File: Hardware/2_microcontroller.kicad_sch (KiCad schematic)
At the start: 27 parts, among them Y1 8Mhz

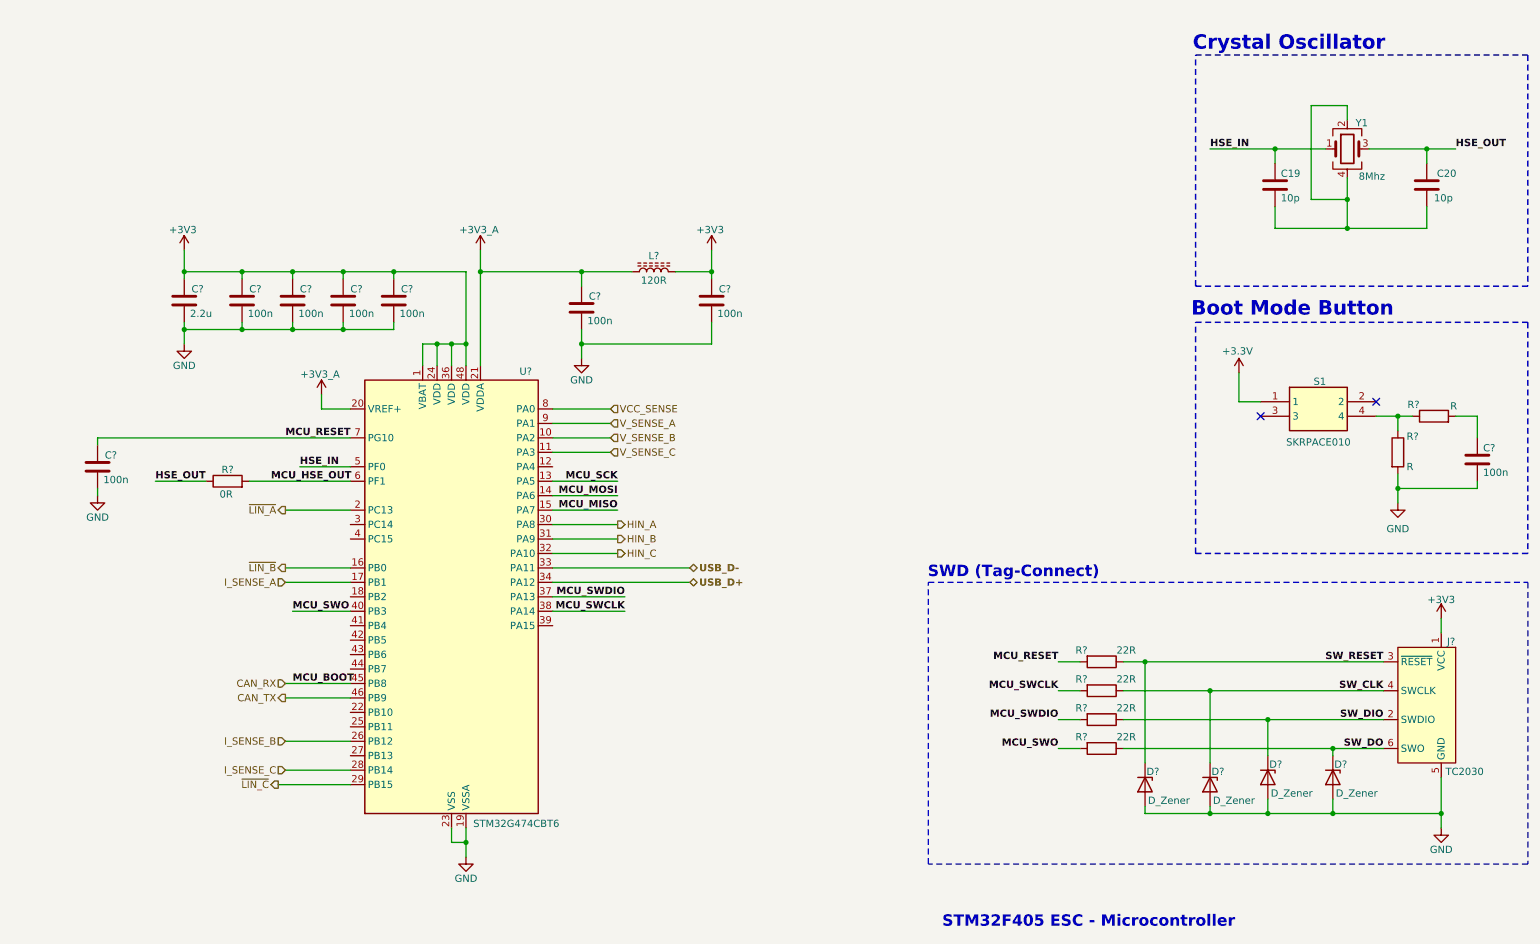
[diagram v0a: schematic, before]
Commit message: feat: Update to use I2C stemma connector
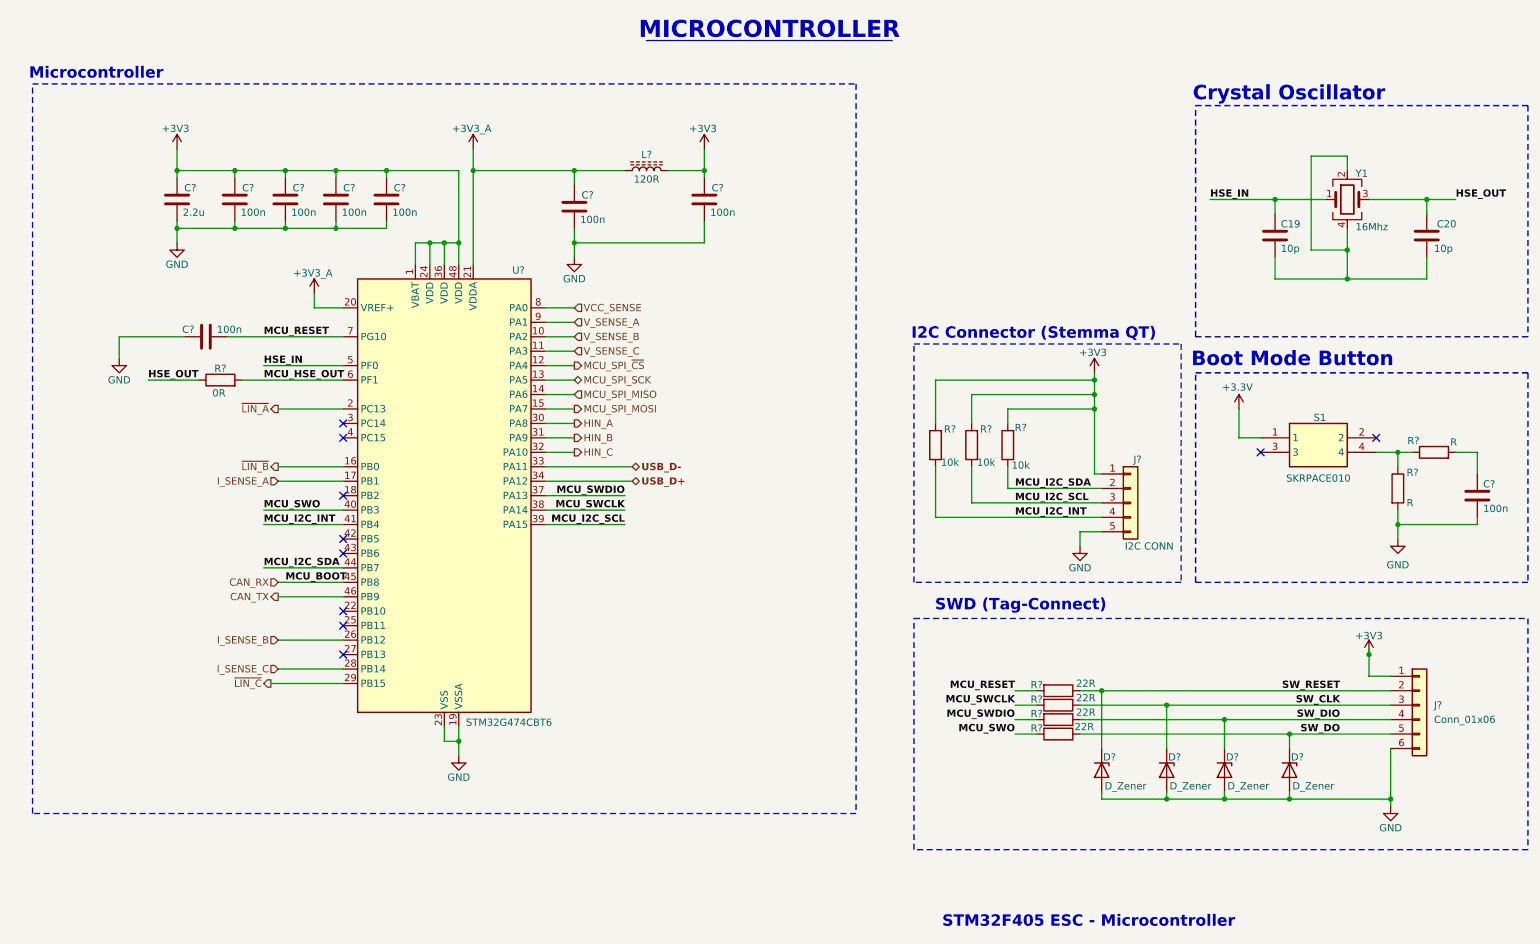
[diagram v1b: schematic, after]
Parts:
- removed J?: TC2030, Connector:Tag-Connect_TC2030-IDC-FP_2x03_P1.27mm_Vertical, symbol Connector:Conn_ARM_SWD_TagConnect_TC2030-NL
- added J?: I2C CONN, symbol Connector_Generic:Conn_01x05
- added J?: Conn_01x06, symbol Connector_Generic:Conn_01x06
- added R? (x3): 10k, symbol No silk screen devices:R
- Y1: value 8Mhz -> 16Mhz
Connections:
- net +3V3: now also J?.1 (Pin_1), J?.1 (Pin_1), R?.2, R?.2, R?.2
- net GND: now also C?.1, J?.5 (Pin_5), J?.6 (Pin_6); no longer C?.2
- net MCU_RESET: now also C?.2; no longer C?.1
- net SW_CLK: now also J?.3 (Pin_3)
- net SW_DIO: now also J?.4 (Pin_4)
- net SW_DO: now also J?.5 (Pin_5)
- net SW_RESET: now also J?.2 (Pin_2)
- net MCU_SPI_~{CS}: now reaches U?.12 (PA4)
- net MCU_I2C_SCL: now reaches U?.39 (PA15)
- net MCU_I2C_SCL: now also J?.3 (Pin_3), R?.1
- net MCU_I2C_INT: now reaches U?.41 (PB4)
- net MCU_I2C_INT: now also J?.4 (Pin_4), R?.1
- net MCU_I2C_SDA: now reaches U?.44 (PB7)
- net MCU_I2C_SDA: now also J?.2 (Pin_2), R?.1
- net MCU_MISO renamed MCU_SPI_MOSI
- net MCU_MOSI renamed MCU_SPI_MISO
- net MCU_SCK renamed MCU_SPI_SCK
- no-connect marks 2 -> 10
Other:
- note added: "I2C Connector (Stemma QT)"
- note added: "MICROCONTROLLER"
- note added: "Microcontroller"
- moved on the sheet: C19, C20, C?, D?, L?, R?, S1, U?, Y1
